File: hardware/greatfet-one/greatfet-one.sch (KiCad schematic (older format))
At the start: 88 parts, among them J1 NEIGHBOR1, J2 NEIGHBOR2, J3 USB-MICRO-B-SHIELDED, J4 USB-MICRO-B-SHIELDED, J5 JTAG, J7 BONUS_ROW, SW1 DFU, SW2 RESET, U1 LPC4330FBD144, U2 W25Q16DV, U3 AP7333, U4 IP4220CZ6, U5 NX5P2553GV, X1 MCU_XTAL, X2 RTC_XTAL

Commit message: GreatFET One: schematic changes permitting power supplied by neighbor
Renamed VBUS on J2 pin 2 to +5V and isolated +5V from USB0_VBUS with D5,
a diode to protect the USB host.  Renamed U1 pin 21 from VBUS to
USB0_SENSE and added a votage divider (R25 and R26) to protect this pin
from voltages greater than 3.6 V in the unusual situation that
USB0_SENSE is present without VCC present.  (This happened and appears
to have resulted in damage when someone applied power to a home-built
unit that had an assembly error.)  Changed USB0_SENSE and USB1_SENSE
voltage divider resistor values so they work even when VBUS is as low as
4.4 V.  Added supply voltage requirements to notes in schematic.

These changes are not represented in the layout yet.
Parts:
- added D5: VBUS_DIODE, symbol D
- added R25: 10k, gsg-modules:0603, symbol R
- added R26: 18k, gsg-modules:0603, symbol R
- R22: value 12.0k -> 18k; Description RES SMD 12K OHM 1% 1/10W 0603 -> (none); Manufacturer Stackpole -> (none); Part Number RMCF0603FT12K0 -> (none)
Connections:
- net GND: now also R26.1
- net USB0_VBUS: now reaches FB1.1, J3.1 (VBUS), U4.5 (VP)
- net VBUS renamed +5V
- net +5V: now also D5.1 (K); no longer FB1.2, U1.21 (USB0_VBUS)
- new net: D5.2 (A), FB1.2, R25.1
- new net USB0_SENSE: R25.2, R26.2, U1.21 (USB0_VBUS)
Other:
- note added: "+5V may have an actual\nvoltage from 3.6 V to 5.25 V.\n\nJ2 pin 2 may be used as\na power input, supplying\n+5V. If so, be prepared for\nUSB0_VBUS (or another\nneighbor supplying +5V) to\nappear, possibly reversing\nthe current on J2 pin 2."
- note added: "+5V should be between\n4.75 V and 5.25 V for\noperation of USB1 in host\nmode."
- note added: "Default boot configuration is SPIFI.\nHold SW1 through reset to boot to\nUSB0 (DFU) mode."
- note added: "USB0_VBUS must be\nbetween 4.4 V and 5.25 V\nbut may be disconnected\nif +5V is supplied via J2."
- note added: "VCC: 3.3 V +/- 2%\nMaximum current: 300 mA"
- note removed: "Default boot configuration is SPIFI.\nPress SW1 during reset to switch to\nUSB0 (DFU) mode."
- note removed: "Maximum current: 300 mA"
- moved on the sheet: C3, C4, FB1, FB2, J3, U3

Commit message: GreatFET One: 18k resistor component selection, R22 and R26
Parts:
- R22, R26: Description (none) -> RES SMD 10K OHM 5% 1/10W 0603; Manufacturer (none) -> Yageo; Part Number (none) -> RC0603JR-0710KL
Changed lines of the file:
@@
 F 2 "gsg-modules:0603" V 13130 4950 30  0001 C CNN
 F 3 "" H 13200 4950 30  0000 C CNN
+F 4 "Yageo" H 13200 4950 60  0001 C CNN "Manufacturer"
+F 5 "RC0603JR-0710KL" H 13200 4950 60  0001 C CNN "Part Number"
+F 6 "RES SMD 10K OHM 5% 1/10W 0603" H 13200 4950 60  0001 C CNN "Description"
 	1    13200 4950
 	-1   0    0    1
@@
 F 2 "gsg-modules:0603" V 2730 6950 30  0001 C CNN
 F 3 "" H 2800 6950 30  0000 C CNN
+F 4 "Yageo" H 2800 6950 60  0001 C CNN "Manufacturer"
+F 5 "RC0603JR-0710KL" H 2800 6950 60  0001 C CNN "Part Number"
+F 6 "RES SMD 10K OHM 5% 1/10W 0603" H 2800 6950 60  0001 C CNN "Description"
 	1    2800 6950
 	-1   0    0    1

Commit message: GreatFET One: updated layout to reflect VBUS changes
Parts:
- D5: footprint (none) -> gsg-modules:B140-13-F

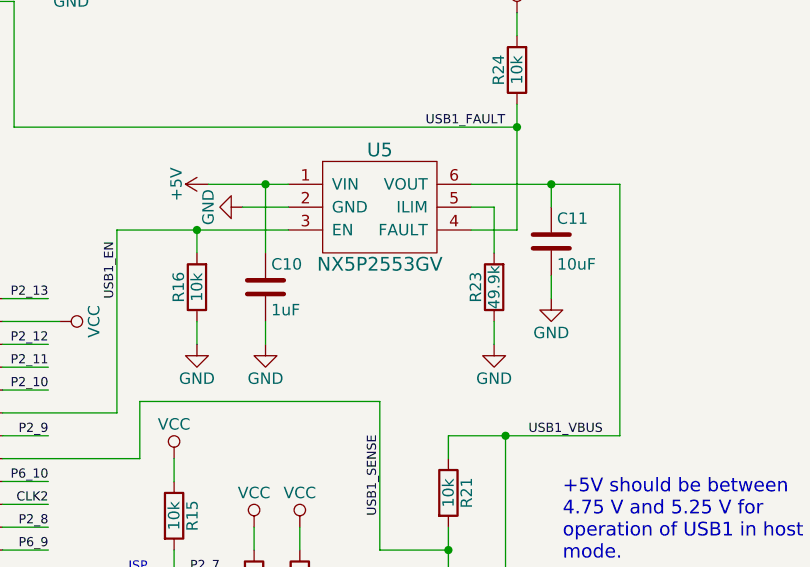
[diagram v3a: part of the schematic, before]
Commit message: GreatFET One: changed U5 from NX5P2553GVH (end of life) to AP2553W6-7, updated ILIM resistor R23
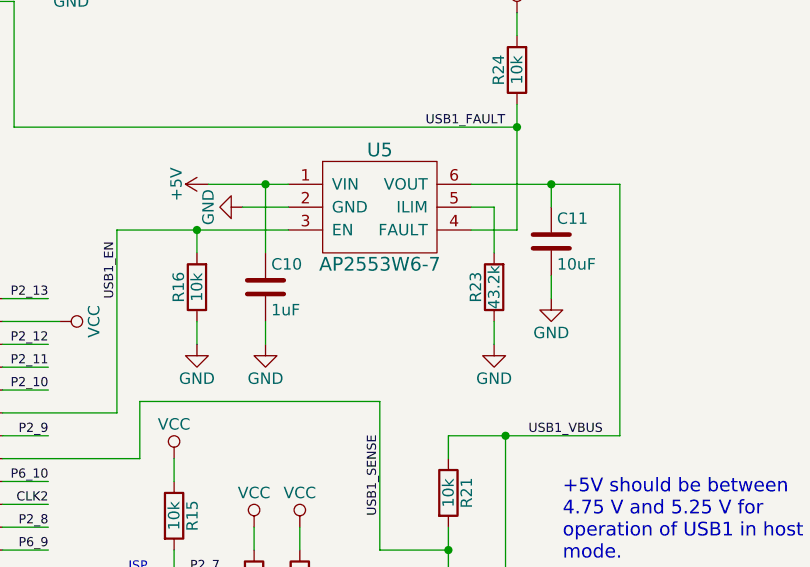
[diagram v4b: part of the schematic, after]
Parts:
- R23: value 49.9k -> 43.2k; Description RES SMD 49.9K OHM 1% 1/10W 0603 -> RES SMD 43.2K OHM 1% 1/10W 0603; Manufacturer Stackpole -> Yageo; Part Number RMCF0603FT49K9 -> RC0603FR-0743K2L
- U5: value NX5P2553GV -> AP2553W6-7; Description IC LOAD SWITCH SC74 -> IC PD SW CURR LIMIT SOT26; Manufacturer NXP -> Diodes Inc.; Part Number NX5P2553GVH -> AP2553W6-7
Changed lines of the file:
@@
 P 12900 3200
 F 0 "U5" H 12900 3450 60  0000 C CNN
-F 1 "NX5P2553GV" H 12900 2950 60  0000 C CNN
+F 1 "AP2553W6-7" H 12900 2950 60  0000 C CNN
 F 2 "gsg-modules:SOT457" H 12900 3200 60  0001 C CNN
 F 3 "" H 12900 3200 60  0000 C CNN
-F 4 "NXP" H 12900 3200 60  0001 C CNN "Manufacturer"
-F 5 "NX5P2553GVH" H 12900 3200 60  0001 C CNN "Part Number"
-F 6 "IC LOAD SWITCH SC74" H 12900 3200 60  0001 C CNN "Description"
+F 4 "Diodes Inc." H 12900 3200 60  0001 C CNN "Manufacturer"
+F 5 "AP2553W6-7" H 12900 3200 60  0001 C CNN "Part Number"
+F 6 "IC PD SW CURR LIMIT SOT26 " H 12900 3200 60  0001 C CNN "Description"
 	1    12900 3200
 	1    0    0    -1
@@
 P 13400 3550
 F 0 "R23" V 13480 3550 50  0000 C CNN
-F 1 "49.9k" V 13400 3550 50  0000 C CNN
+F 1 "43.2k" V 13400 3550 50  0000 C CNN
 F 2 "gsg-modules:0603" V 13330 3550 30  0001 C CNN
 F 3 "" H 13400 3550 30  0000 C CNN
-F 4 "Stackpole" H 13400 3550 60  0001 C CNN "Manufacturer"
-F 5 "RMCF0603FT49K9" H 13400 3550 60  0001 C CNN "Part Number"
-F 6 "RES SMD 49.9K OHM 1% 1/10W 0603" H 13400 3550 60  0001 C CNN "Description"
+F 4 "Yageo" H 13400 3550 60  0001 C CNN "Manufacturer"
+F 5 "RC0603FR-0743K2L" H 13400 3550 60  0001 C CNN "Part Number"
+F 6 "RES SMD 43.2K OHM 1% 1/10W 0603 " H 13400 3550 60  0001 C CNN "Description"
 	1    13400 3550
 	-1   0    0    1

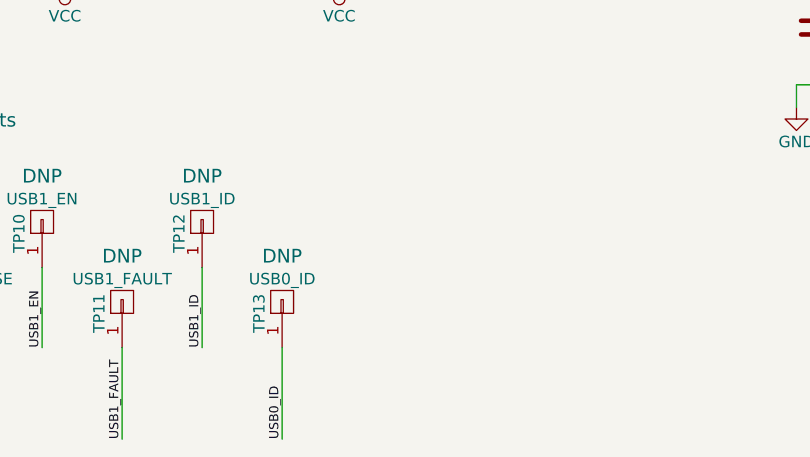
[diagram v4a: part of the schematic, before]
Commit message: GreatFET One: more USB0 test points
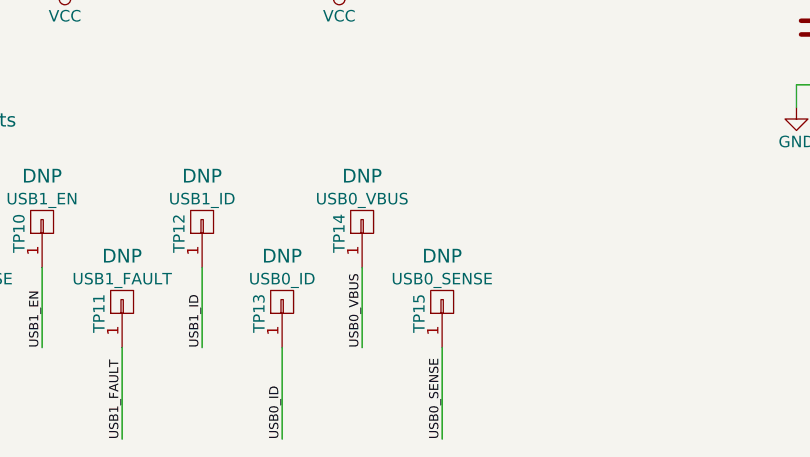
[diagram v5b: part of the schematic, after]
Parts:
- added TP14: USB0_VBUS, gsg-modules:TESTPOINT-50MIL, symbol CONN_01X01
- added TP15: USB0_SENSE, gsg-modules:TESTPOINT-50MIL, symbol CONN_01X01
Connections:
- net USB0_SENSE: now also TP15.1 (P1)
- net USB0_VBUS: now also TP14.1 (P1)

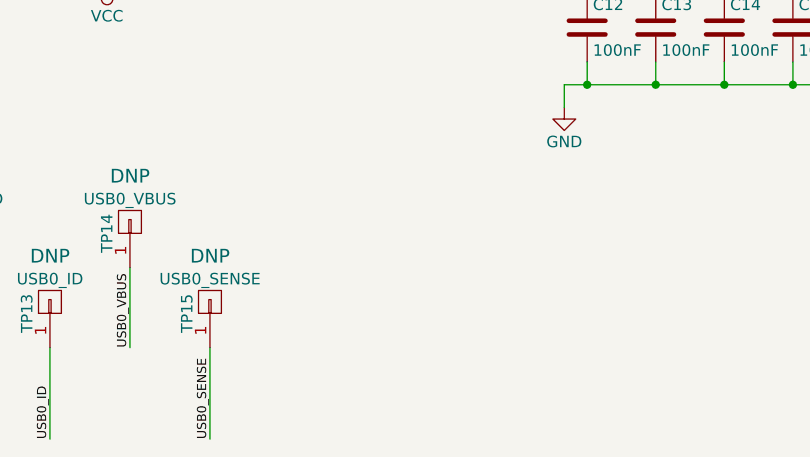
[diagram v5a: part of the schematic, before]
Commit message: GreatFET One: more JTAG test points
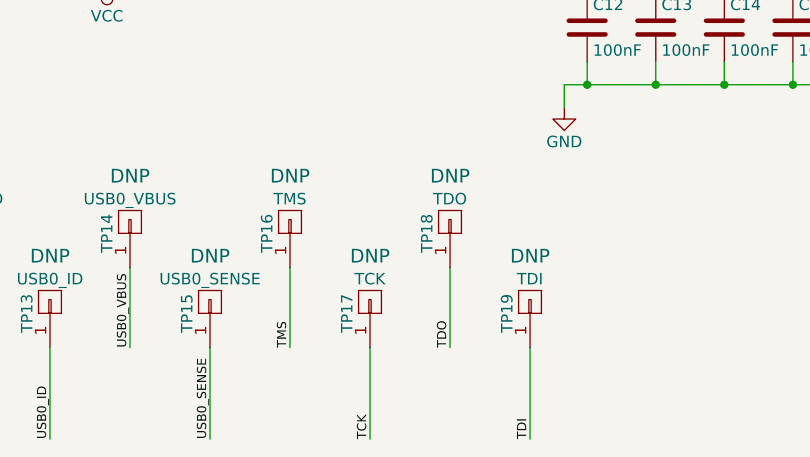
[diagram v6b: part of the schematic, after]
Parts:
- added TP16: TMS, gsg-modules:TESTPOINT-50MIL, symbol CONN_01X01
- added TP17: TCK, gsg-modules:TESTPOINT-50MIL, symbol CONN_01X01
- added TP18: TDO, gsg-modules:TESTPOINT-50MIL, symbol CONN_01X01
- added TP19: TDI, gsg-modules:TESTPOINT-50MIL, symbol CONN_01X01
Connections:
- net TCK: now also TP17.1 (P1)
- net TDI: now also TP19.1 (P1)
- net TDO: now also TP18.1 (P1)
- net TMS: now also TP16.1 (P1)
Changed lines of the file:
@@
 Wire Wire Line
 	10650 10250 10650 9850
+Text Label 11000 9850 1    40   ~ 0
+TMS
+$Comp
+L CONN_01X01 TP16
+U 1 1 57C57DEC
+P 11000 9300
+F 0 "TP16" H 10950 9400 50  0000 C CNN
+F 1 "TMS" V 11100 9300 50  0000 C CNN
+F 2 "gsg-modules:TESTPOINT-50MIL" H 11000 9300 60  0001 C CNN
+F 3 "" H 11000 9300 60  0000 C CNN
+F 4 "DNP" V 11200 9300 60  0000 C CNN "Note"
+	1    11000 9300
+	0    -1   -1   0
+$EndComp
+$Comp
+L CONN_01X01 TP17
+U 1 1 57C57DF3
+P 11350 9650
+F 0 "TP17" H 11300 9750 50  0000 C CNN
+F 1 "TCK" V 11450 9650 50  0000 C CNN
+F 2 "gsg-modules:TESTPOINT-50MIL" H 11350 9650 60  0001 C CNN
+F 3 "" H 11350 9650 60  0000 C CNN
+F 4 "DNP" V 11550 9650 60  0000 C CNN "Note"
+	1    11350 9650
+	0    -1   -1   0
+$EndComp
+Text Label 11350 10250 1    40   ~ 0
+TCK
+Wire Wire Line
+	11000 9850 11000 9500
+Wire Wire Line
+	11350 10250 11350 9850
+$Comp
+L CONN_01X01 TP18
+U 1 1 57C57DFD
+P 11700 9300
+F 0 "TP18" H 11650 9400 50  0000 C CNN
+F 1 "TDO" V 11800 9300 50  0000 C CNN
+F 2 "gsg-modules:TESTPOINT-50MIL" H 11700 9300 60  0001 C CNN
+F 3 "" H 11700 9300 60  0000 C CNN
+F 4 "DNP" V 11900 9300 60  0000 C CNN "Note"
+	1    11700 9300
+	0    -1   -1   0
+$EndComp
+Text Label 11700 9850 1    40   ~ 0
+TDO
+$Comp
+L CONN_01X01 TP19
+U 1 1 57C57E05
+P 12050 9650
+F 0 "TP19" H 12000 9750 50  0000 C CNN
+F 1 "TDI" V 12150 9650 50  0000 C CNN
+F 2 "gsg-modules:TESTPOINT-50MIL" H 12050 9650 60  0001 C CNN
+F 3 "" H 12050 9650 60  0000 C CNN
+F 4 "DNP" V 12250 9650 60  0000 C CNN "Note"
+	1    12050 9650
+	0    -1   -1   0
+$EndComp
+Text Label 12050 10250 1    40   ~ 0
+TDI
+Wire Wire Line
+	11700 9850 11700 9500
+Wire Wire Line
+	12050 10250 12050 9850
 $EndSCHEMATC

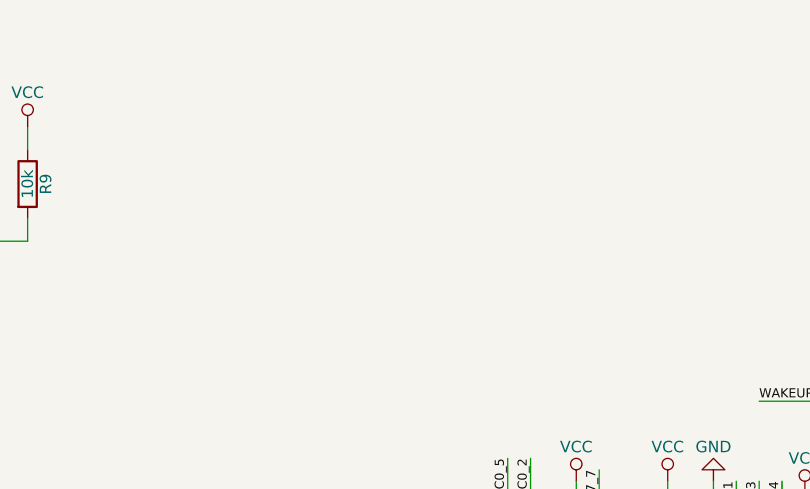
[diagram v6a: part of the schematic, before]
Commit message: GreatFET One: J6 POWER header on bottom, can be used with single row header on edge, could be useful for non-USB applications of U5 power switch
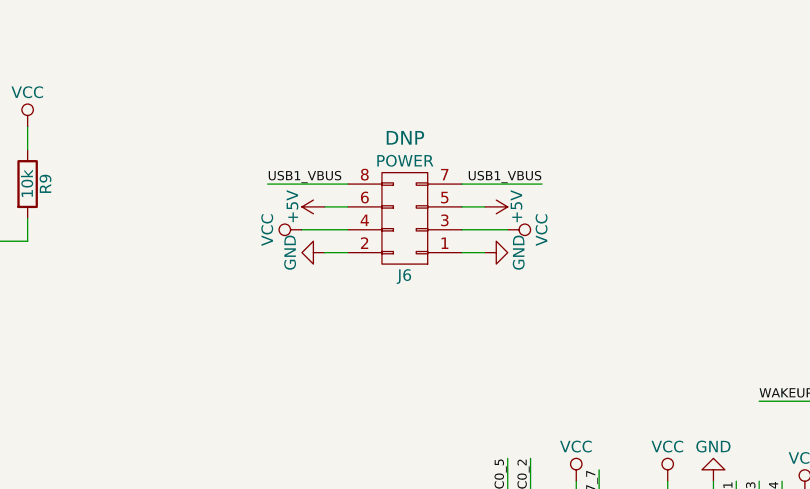
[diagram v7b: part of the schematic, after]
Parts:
- added J6: POWER, gsg-modules:HEADER-SMT-2x4, symbol CONN_02X04
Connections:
- net +5V: now also J6.5 (P5), J6.6 (P6)
- net GND: now also J6.1 (P1), J6.2 (P2)
- net USB1_VBUS: now also J6.7 (P7), J6.8 (P8)
- net VCC: now also J6.3 (P3), J6.4 (P4)
